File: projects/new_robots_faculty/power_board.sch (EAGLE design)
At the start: 46 parts

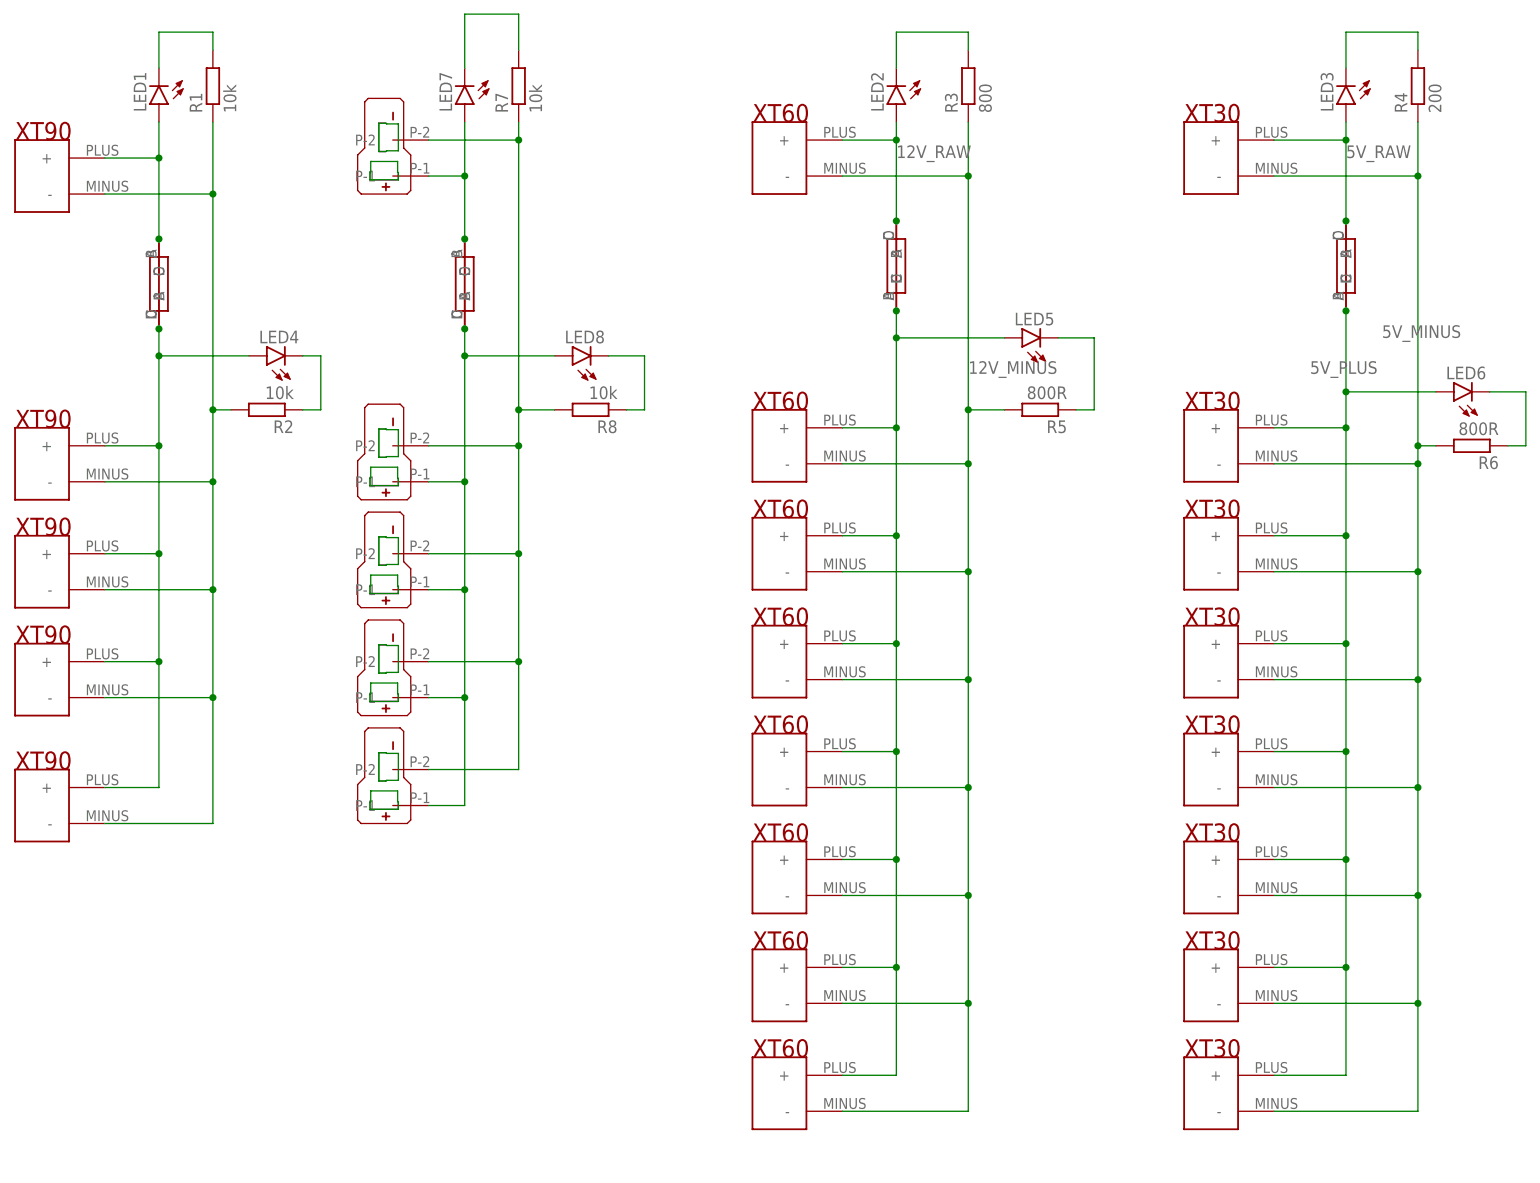
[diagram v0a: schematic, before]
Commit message: miniaturized chassis board
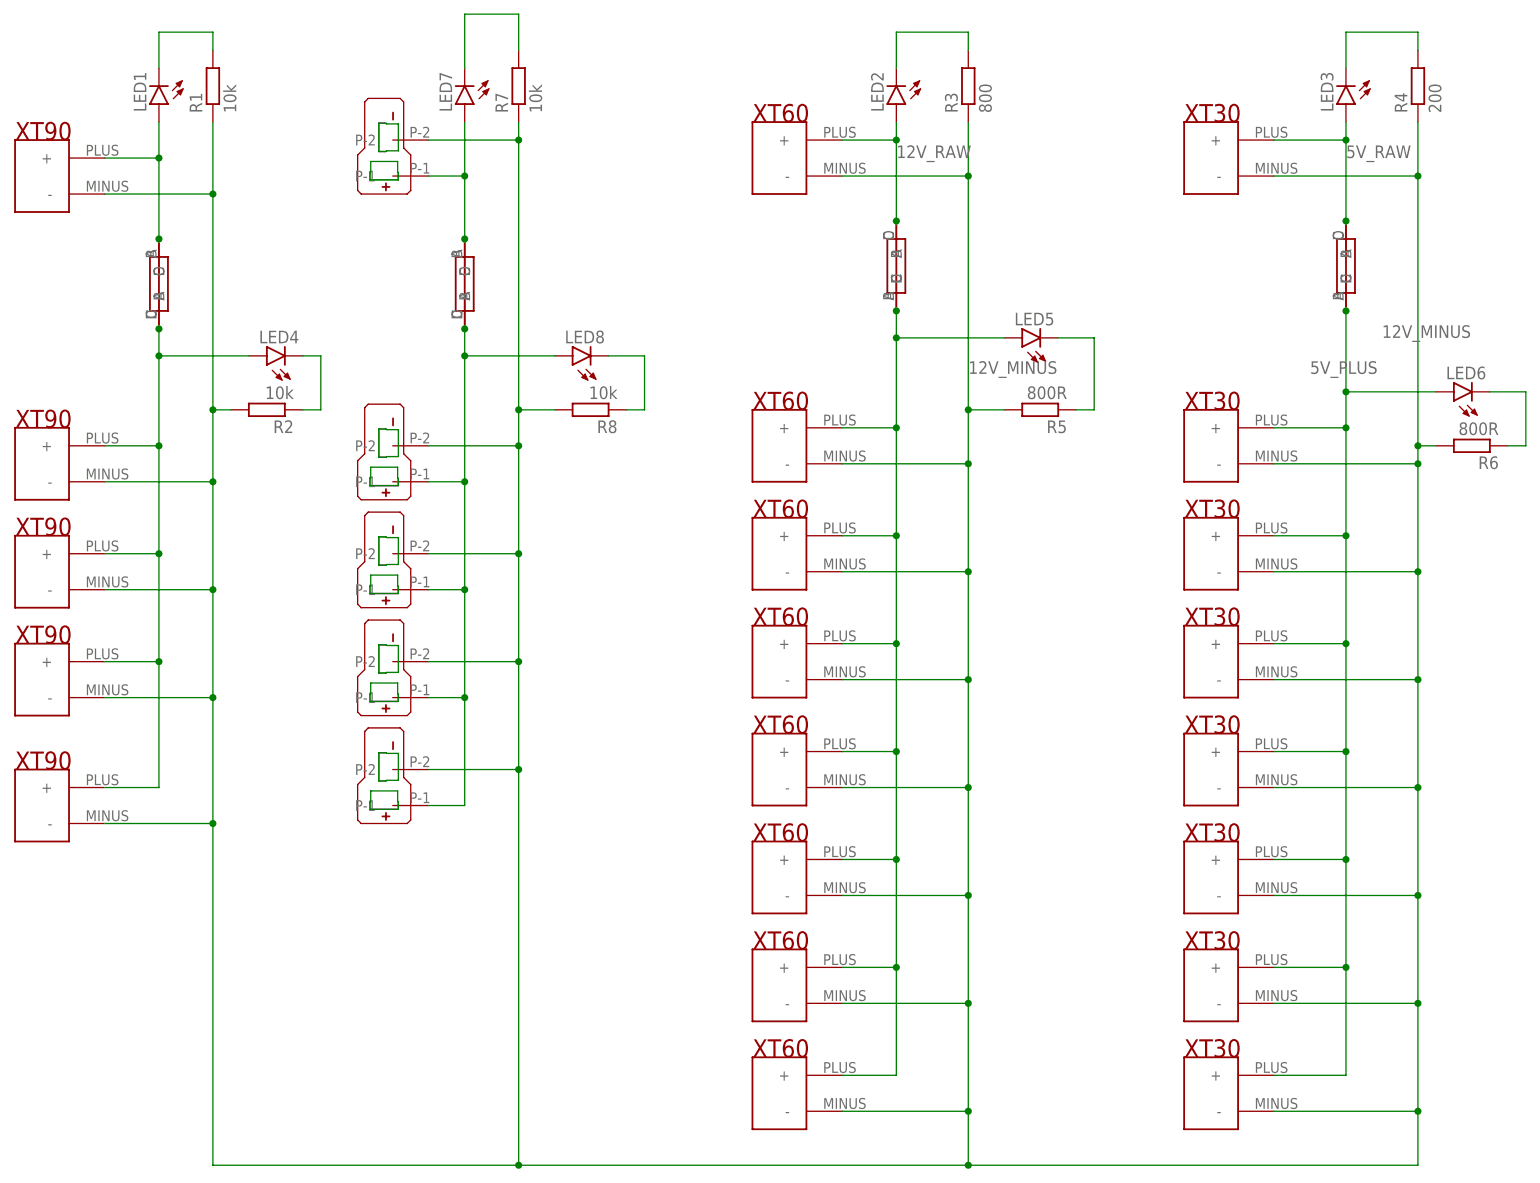
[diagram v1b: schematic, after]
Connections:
- removed net 5V_MINUS: R4.1, R6.2, U$13.-, U$14.-, U$15.-, U$16.-, U$17.-, U$18.-, U$19.-, U$20.-
- removed net BATT_MINUS: R1.1, R2.2, U$1.-, U$2.-, U$24.-, U$3.-, U$4.-
- removed net N$11: R7.1, R8.2, U$25.P-2, U$26.P-2, U$27.P-2, U$28.P-2, U$29.P-2
- net 12V_MINUS: now also R1.1, R2.2, R4.1, R6.2, R7.1, R8.2, U$1.-, U$13.-, U$14.-, U$15.-, U$16.-, U$17.-, U$18.-, U$19.-, U$2.-, U$20.-, U$24.-, U$25.P-2, U$26.P-2, U$27.P-2, U$28.P-2, U$29.P-2, U$3.-, U$4.-

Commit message: updated asgard power board
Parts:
- added U$31, U$32, U$33: T-PLUG_CONNECTOR, con-T-plug:T-PLUG_CONNECTOR
- added U$34: XT90, XT_connectors:XT90
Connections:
- net 12V_MINUS: now also U$31.P-2, U$32.P-2, U$33.P-2, U$34.-
- net BATT_PLUS: now also U$34.+
- net N$12: now also U$31.P-1, U$32.P-1, U$33.P-1
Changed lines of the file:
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@@
 <?xml version="1.0" encoding="utf-8"?>
 <!DOCTYPE eagle SYSTEM "eagle.dtd">
-<eagle version="9.6.2">
+<eagle version="9.3.2">
 <drawing>
 <settings>
@@
 <part name="LED8" library="led" library_urn="urn:adsk.eagle:library:259" deviceset="LED" device="5MM" package3d_urn="urn:adsk.eagle:package:15799/2"/>
 <part name="R8" library="rcl" library_urn="urn:adsk.eagle:library:334" deviceset="R-EU_" device="M1206" package3d_urn="urn:adsk.eagle:package:23566/2" value="10k"/>
+<part name="U$31" library="con-T-plug" deviceset="T-PLUG_CONNECTOR" device=""/>
+<part name="U$32" library="con-T-plug" deviceset="T-PLUG_CONNECTOR" device=""/>
+<part name="U$33" library="con-T-plug" deviceset="T-PLUG_CONNECTOR" device=""/>
+<part name="U$34" library="XT_connectors" deviceset="XT90" device=""/>
 </parts>
 <sheets>
@@
 <attribute name="VALUE" x="41.91" y="79.502" size="1.778" layer="96" rot="R180"/>
 </instance>
+<instance part="U$31" gate="T_PLUG" x="12.7" y="2.54" smashed="yes" rot="R90"/>
+<instance part="U$32" gate="T_PLUG" x="12.7" y="-12.7" smashed="yes" rot="R90"/>
+<instance part="U$33" gate="T_PLUG" x="12.7" y="-27.94" smashed="yes" rot="R90"/>
+<instance part="U$34" gate="G$1" x="-40.64" y="2.54" smashed="yes"/>
 </instances>
 <busses>
@@
 <pinref part="U$21" gate="G$1" pin="C"/>
 <pinref part="LED4" gate="G$1" pin="A"/>
+<pinref part="U$34" gate="G$1" pin="+"/>
+<wire x1="-30.48" y1="5.08" x2="-22.86" y2="5.08" width="0.1524" layer="91"/>
+<wire x1="-22.86" y1="5.08" x2="-22.86" y2="22.86" width="0.1524" layer="91"/>
+<junction x="-22.86" y="22.86"/>
 </segment>
 </net>
@@
 <wire x1="91.44" y1="-30.48" x2="27.94" y2="-30.48" width="0.1524" layer="91"/>
 <wire x1="27.94" y1="-30.48" x2="-15.24" y2="-30.48" width="0.1524" layer="91"/>
-<wire x1="-15.24" y1="-30.48" x2="-15.24" y2="17.78" width="0.1524" layer="91"/>
+<wire x1="-15.24" y1="-30.48" x2="-15.24" y2="0" width="0.1524" layer="91"/>
 <pinref part="R1" gate="G$1" pin="1"/>
+<wire x1="-15.24" y1="0" x2="-15.24" y2="17.78" width="0.1524" layer="91"/>
 <wire x1="-15.24" y1="116.84" x2="-15.24" y2="106.68" width="0.1524" layer="91"/>
 <pinref part="U$1" gate="G$1" pin="-"/>
@@
 <wire x1="33.02" y1="76.2" x2="27.94" y2="76.2" width="0.1524" layer="91"/>
 <junction x="27.94" y="76.2"/>
-<wire x1="27.94" y1="25.4" x2="27.94" y2="-30.48" width="0.1524" layer="91"/>
+<wire x1="27.94" y1="25.4" x2="27.94" y2="10.16" width="0.1524" layer="91"/>
 <junction x="27.94" y="25.4"/>
 <junction x="27.94" y="-30.48"/>
+<wire x1="27.94" y1="10.16" x2="27.94" y2="-5.08" width="0.1524" layer="91"/>
+<wire x1="27.94" y1="-5.08" x2="27.94" y2="-20.32" width="0.1524" layer="91"/>
+<wire x1="27.94" y1="-20.32" x2="27.94" y2="-30.48" width="0.1524" layer="91"/>
 <wire x1="91.44" y1="-22.86" x2="91.44" y2="-30.48" width="0.1524" layer="91"/>
 <junction x="91.44" y="-22.86"/>
 <junction x="91.44" y="-30.48"/>
+<pinref part="U$34" gate="G$1" pin="-"/>
+<wire x1="-30.48" y1="0" x2="-15.24" y2="0" width="0.1524" layer="91"/>
+<junction x="-15.24" y="0"/>
+<pinref part="U$31" gate="T_PLUG" pin="P-2"/>
+<wire x1="15.24" y1="10.16" x2="27.94" y2="10.16" width="0.1524" layer="91"/>
+<junction x="27.94" y="10.16"/>
+<pinref part="U$32" gate="T_PLUG" pin="P-2"/>
+<wire x1="15.24" y1="-5.08" x2="27.94" y2="-5.08" width="0.1524" layer="91"/>
+<junction x="27.94" y="-5.08"/>
+<pinref part="U$33" gate="T_PLUG" pin="P-2"/>
+<wire x1="15.24" y1="-20.32" x2="27.94" y2="-20.32" width="0.1524" layer="91"/>
+<junction x="27.94" y="-20.32"/>
 </segment>
 </net>
@@
 <wire x1="33.02" y1="83.82" x2="20.32" y2="83.82" width="0.1524" layer="91"/>
 <junction x="20.32" y="83.82"/>
-</segment>
-</net>
+<pinref part="U$33" gate="T_PLUG" pin="P-1"/>
+<wire x1="15.24" y1="-25.4" x2="20.32" y2="-25.4" width="0.1524" layer="91"/>
+<wire x1="20.32" y1="-25.4" x2="20.32" y2="-10.16" width="0.1524" layer="91"/>
+<junction x="20.32" y="20.32"/>
+<pinref part="U$32" gate="T_PLUG" pin="P-1"/>
+<wire x1="20.32" y1="-10.16" x2="20.32" y2="5.08" width="0.1524" layer="91"/>
+<wire x1="20.32" y1="5.08" x2="20.32" y2="20.32" width="0.1524" layer="91"/>
+<wire x1="15.24" y1="-10.16" x2="20.32" y2="-10.16" width="0.1524" layer="91"/>
+<junction x="20.32" y="-10.16"/>
+<pinref part="U$31" gate="T_PLUG" pin="P-1"/>
+<wire x1="15.24" y1="5.08" x2="20.32" y2="5.08" width="0.1524" layer="91"/>
+<junction x="20.32" y="5.08"/>
+</segment>
+</net>
